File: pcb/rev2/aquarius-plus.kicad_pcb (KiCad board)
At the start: 2 copper layers, 167 x 115 mm, 173 parts, among them J1 Power in, J10 FPGA spare, J11 Hand controller 2, J12 Hand controller 1, J13 ESP32 spare, J2 ESP USB Host, J3 Audio out, J4 VGA, J5 Cassette out, J6 Cassette in, J7 Expansion port, J8 Printer, J9 TF-03A, Q1 BC847C, Q2 BC847C, Q3 2N7002, SW1 SW_DPDT_x2, U1 SN74AHCT1G125DBVR, U10 ESP32-S3-WROOM-1-N4R2, U11 LDL1117S33R, U12 SN74CB3T3245PWR, U13 IS61C5128AS-25QLI, U2 SN74AHCT1G125DBVR, U3 LD1117S12, U4 SN74CB3T3245PWR, U5 MAX3221ECPWR, U6 XC6SLX9-2TQG144C, U7 Z84C0010AEG, U8 SN74CB3T3245PWR, U9 SN74CB3T3245PWR, X1 SX3M14.31818M20F30TNN

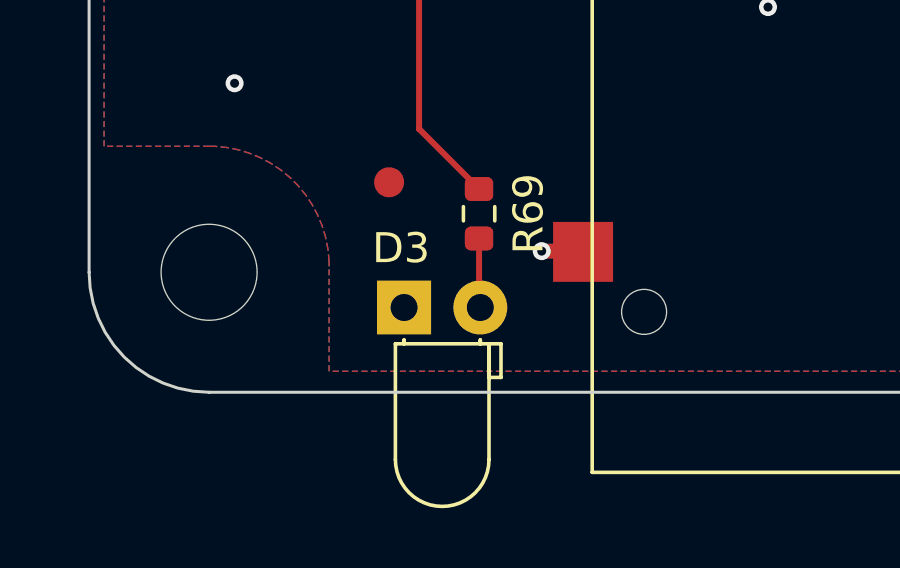
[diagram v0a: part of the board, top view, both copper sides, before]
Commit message: PCB rev2 Tweaks for LED polarity
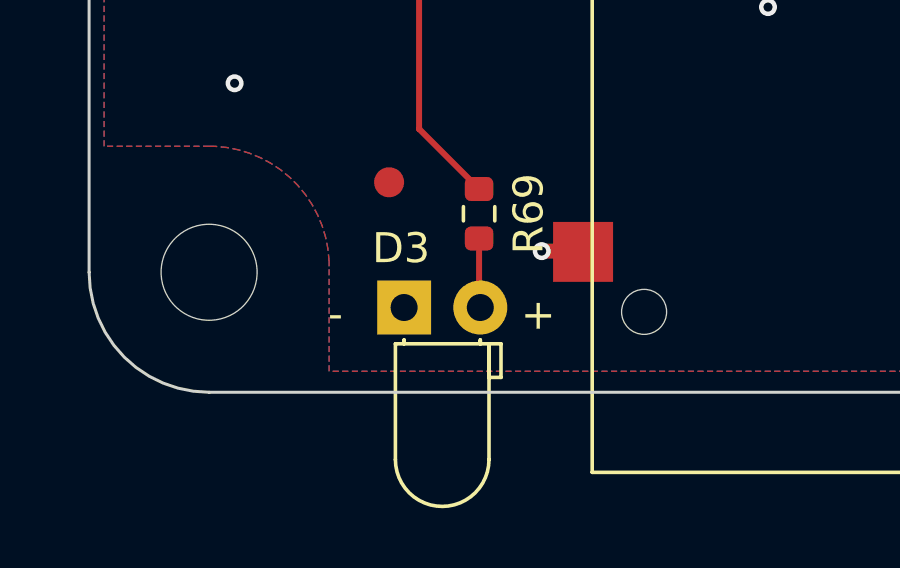
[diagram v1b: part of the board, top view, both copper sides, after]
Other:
- board text added: "+"
- board text added: "-"
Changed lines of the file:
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@@
     (effects (font (size 1.5 1.5) (thickness 0.3)))
+  )
+  (gr_text "-" (at 72.964539 147.399272) (layer "F.SilkS")
+    (effects (font (size 1 1) (thickness 0.15)) (justify left))
   )
   (gr_text "Audio Out" (at 132 47.5 90) (layer "F.SilkS")
@@
     (effects (font (size 2 2) (thickness 0.3)))
   )
+  (gr_text "+" (at 79.395539 147.419623) (layer "F.SilkS")
+    (effects (font (size 1 1) (thickness 0.15)) (justify left))
+  )
   (gr_text "Power" (at 80.133319 42.362823) (layer "F.SilkS")

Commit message: Renaming SPI nets to match the software.
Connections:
- U10 pad 15: SPI_MISO -> SPI_CS#
- U10 pad 19: SPI_CS# -> SPI_MISO
- U6 pad 39: SPI_MISO -> SPI_CS#
- U6 pad 74: SPI_CS# -> SPI_MISO
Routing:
- net SPI_MISO: track 53.2 -> 45.3 mm, vias 4 -> 0
- net SPI_CS#: track 45.3 -> 53.2 mm, vias 0 -> 4
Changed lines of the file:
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@@
       (net 41 "CASSETTE_OUT") (pinfunction "B2_IO") (pintype "passive"))
     (pad "39" smd roundrect (at -7.75 10.6625 270) (size 0.3 1.475) (layers "F.Cu" "F.Paste" "F.Mask") (roundrect_rratio 0.25)
-      (net 96 "SPI_MISO") (pinfunction "B2_IO_INIT_B") (pintype "passive"))
+      (net 28 "SPI_CS#") (pinfunction "B2_IO_INIT_B") (pintype "passive"))
     (pad "40" smd roundrect (at -7.25 10.6625 270) (size 0.3 1.475) (layers "F.Cu" "F.Paste" "F.Mask") (roundrect_rratio 0.25)
       (net 26 "CASSETTE_IN") (pinfunction "B2_IO") (pintype "passive"))
@@
       (net 2 "GND") (pinfunction "SUSPEND") (pintype "input"))
     (pad "74" smd roundrect (at 10.6625 8.25 270) (size 1.475 0.3) (layers "F.Cu" "F.Paste" "F.Mask") (roundrect_rratio 0.25)
-      (net 28 "SPI_CS#") (pinfunction "B2_IO_DOUT") (pintype "passive"))
+      (net 96 "SPI_MISO") (pinfunction "B2_IO_DOUT") (pintype "passive"))
     (pad "75" smd roundrect (at 10.6625 7.75 270) (size 1.475 0.3) (layers "F.Cu" "F.Paste" "F.Mask") (roundrect_rratio 0.25)
       (net 66 "HC1_D00") (pinfunction "B1_IO_AWAKE") (pintype "passive"))
@@
       (net 25 "ESP_USB_D+") (pinfunction "IO20/USB_DP") (pintype "bidirectional"))
     (pad "15" smd roundrect locked (at -6.985 25.25 270) (size 0.9 1.5) (layers "F.Cu" "F.Paste" "F.Mask") (roundrect_rratio 0.25)
-      (net 96 "SPI_MISO") (pinfunction "IO3") (pintype "bidirectional"))
+      (net 28 "SPI_CS#") (pinfunction "IO3") (pintype "bidirectional"))
     (pad "16" smd roundrect locked (at -5.715 25.25 270) (size 0.9 1.5) (layers "F.Cu" "F.Paste" "F.Mask") (roundrect_rratio 0.25)
       (net 243 "unconnected-(U10-IO46{slash}I-Pad16)") (pinfunction "IO46/I") (pintype "input+no_connect"))
@@
       (net 33 "SPI_SCLK") (pinfunction "IO10") (pintype "bidirectional"))
     (pad "19" smd roundrect locked (at -1.905 25.25 270) (size 0.9 1.5) (layers "F.Cu" "F.Paste" "F.Mask") (roundrect_rratio 0.25)
-      (net 28 "SPI_CS#") (pinfunction "IO11") (pintype "bidirectional"))
+      (net 96 "SPI_MISO") (pinfunction "IO11") (pintype "bidirectional"))
     (pad "20" smd roundrect locked (at -0.635 25.25 270) (size 0.9 1.5) (layers "F.Cu" "F.Paste" "F.Mask") (roundrect_rratio 0.25)
       (net 94 "ESP_NOTIFY") (pinfunction "IO12") (pintype "bidirectional"))
@@
   (segment (start 114.400499 84.231011) (end 114.132509 84.499001) (width 0.2) (layer "B.Cu") (net 26))
   (segment (start 88.0125 69.1) (end 83.325 69.1) (width 0.3) (layer "F.Cu") (net 27))
-  (segment (start 126.97 103.875) (end 126.97 104.83) (width 0.2) (layer "F.Cu") (net 28))
-  (segment (start 92.497908 107.905) (end 90.25 107.905) (width 0.2) (layer "F.Cu") (net 28))
-  (segment (start 116.41498 100.4) (end 113.46498 97.45) (width 0.2) (layer "F.Cu") (net 28))
-  (segment (start 118.353218 100.4) (end 116.41498 100.4) (width 0.2) (layer "F.Cu") (net 28))
-  (segment (start 125.75 105.1) (end 124.75 104.1) (width 0.2) (layer "F.Cu") (net 28))
-  (segment (start 126.97 104.83) (end 126.7 105.1) (width 0.2) (layer "F.Cu") (net 28))
-  (segment (start 102.952908 97.45) (end 92.497908 107.905) (width 0.2) (layer "F.Cu") (net 28))
-  (segment (start 126.7 105.1) (end 125.75 105.1) (width 0.2) (layer "F.Cu") (net 28))
-  (segment (start 122.053218 104.1) (end 118.353218 100.4) (width 0.2) (layer "F.Cu") (net 28))
-  (segment (start 113.46498 97.45) (end 102.952908 97.45) (width 0.2) (layer "F.Cu") (net 28))
-  (segment (start 124.75 104.1) (end 122.053218 104.1) (width 0.2) (layer "F.Cu") (net 28))
+  (segment (start 124.5575 85.4625) (end 123.0625 85.4625) (width 0.2) (layer "F.Cu") (net 28))
+  (segment (start 113.7 85.8) (end 110.6 85.8) (width 0.2) (layer "F.Cu") (net 28))
+  (segment (start 90.25 112.985) (end 91.55 112.985) (width 0.2) (layer "F.Cu") (net 28))
+  (segment (start 123.0625 85.4625) (end 122.9 85.3) (width 0.2) (layer "F.Cu") (net 28))
+  (segment (start 116.5005 85.3) (end 116.3 85.0995) (width 0.2) (layer "F.Cu") (net 28))
+  (segment (start 110.6 85.8) (end 96.55 99.85) (width 0.2) (layer "F.Cu") (net 28))
+  (segment (start 96.55 99.85) (end 93.15 99.85) (width 0.2) (layer "F.Cu") (net 28))
+  (segment (start 122.9 85.3) (end 116.5005 85.3) (width 0.2) (layer "F.Cu") (net 28))
+  (segment (start 93.15 99.85) (end 92.95 99.65) (width 0.2) (layer "F.Cu") (net 28))
+  (via (at 113.7 85.8) (size 0.6) (drill 0.3) (layers "F.Cu" "B.Cu") (net 28))
+  (via (at 116.3 85.0995) (size 0.6) (drill 0.3) (layers "F.Cu" "B.Cu") (net 28))
+  (via (at 91.55 112.985) (size 0.6) (drill 0.3) (layers "F.Cu" "B.Cu") (net 28))
+  (via (at 92.95 99.65) (size 0.6) (drill 0.3) (layers "F.Cu" "B.Cu") (net 28))
+  (segment (start 113.7 85.8) (end 115.5995 85.8) (width 0.2) (layer "B.Cu") (net 28))
+  (segment (start 92.95 99.65) (end 92.95 111.585) (width 0.2) (layer "B.Cu") (net 28))
+  (segment (start 92.95 111.585) (end 91.55 112.985) (width 0.2) (layer "B.Cu") (net 28))
+  (segment (start 115.5995 85.8) (end 116.3 85.0995) (width 0.2) (layer "B.Cu") (net 28))
   (segment (start 84.75 125.4) (end 83.8414 124.4914) (width 0.2) (layer "F.Cu") (net 29))
   (segment (start 98.28 123.07) (end 98.28 124.42) (width 0.2) (layer "F.Cu") (net 29))
@@
   (segment (start 123.3875 93.4625) (end 122.87 93.98) (width 0.2) (layer "F.Cu") (net 95))
   (segment (start 124.5575 93.4625) (end 123.3875 93.4625) (width 0.2) (layer "F.Cu") (net 95))
-  (segment (start 124.5575 85.4625) (end 123.0625 85.4625) (width 0.2) (layer "F.Cu") (net 96))
-  (segment (start 113.7 85.8) (end 110.6 85.8) (width 0.2) (layer "F.Cu") (net 96))
-  (segment (start 90.25 112.985) (end 91.55 112.985) (width 0.2) (layer "F.Cu") (net 96))
-  (segment (start 123.0625 85.4625) (end 122.9 85.3) (width 0.2) (layer "F.Cu") (net 96))
-  (segment (start 116.5005 85.3) (end 116.3 85.0995) (width 0.2) (layer "F.Cu") (net 96))
-  (segment (start 110.6 85.8) (end 96.55 99.85) (width 0.2) (layer "F.Cu") (net 96))
-  (segment (start 96.55 99.85) (end 93.15 99.85) (width 0.2) (layer "F.Cu") (net 96))
-  (segment (start 122.9 85.3) (end 116.5005 85.3) (width 0.2) (layer "F.Cu") (net 96))
-  (segment (start 93.15 99.85) (end 92.95 99.65) (width 0.2) (layer "F.Cu") (net 96))
-  (via (at 113.7 85.8) (size 0.6) (drill 0.3) (layers "F.Cu" "B.Cu") (net 96))
-  (via (at 116.3 85.0995) (size 0.6) (drill 0.3) (layers "F.Cu" "B.Cu") (net 96))
-  (via (at 91.55 112.985) (size 0.6) (drill 0.3) (layers "F.Cu" "B.Cu") (net 96))
-  (via (at 92.95 99.65) (size 0.6) (drill 0.3) (layers "F.Cu" "B.Cu") (net 96))
-  (segment (start 113.7 85.8) (end 115.5995 85.8) (width 0.2) (layer "B.Cu") (net 96))
-  (segment (start 92.95 99.65) (end 92.95 111.585) (width 0.2) (layer "B.Cu") (net 96))
-  (segment (start 92.95 111.585) (end 91.55 112.985) (width 0.2) (layer "B.Cu") (net 96))
-  (segment (start 115.5995 85.8) (end 116.3 85.0995) (width 0.2) (layer "B.Cu") (net 96))
+  (segment (start 126.97 103.875) (end 126.97 104.83) (width 0.2) (layer "F.Cu") (net 96))
+  (segment (start 92.497908 107.905) (end 90.25 107.905) (width 0.2) (layer "F.Cu") (net 96))
+  (segment (start 116.41498 100.4) (end 113.46498 97.45) (width 0.2) (layer "F.Cu") (net 96))
+  (segment (start 118.353218 100.4) (end 116.41498 100.4) (width 0.2) (layer "F.Cu") (net 96))
+  (segment (start 125.75 105.1) (end 124.75 104.1) (width 0.2) (layer "F.Cu") (net 96))
+  (segment (start 126.97 104.83) (end 126.7 105.1) (width 0.2) (layer "F.Cu") (net 96))
+  (segment (start 102.952908 97.45) (end 92.497908 107.905) (width 0.2) (layer "F.Cu") (net 96))
+  (segment (start 126.7 105.1) (end 125.75 105.1) (width 0.2) (layer "F.Cu") (net 96))
+  (segment (start 122.053218 104.1) (end 118.353218 100.4) (width 0.2) (layer "F.Cu") (net 96))
+  (segment (start 113.46498 97.45) (end 102.952908 97.45) (width 0.2) (layer "F.Cu") (net 96))
+  (segment (start 124.75 104.1) (end 122.053218 104.1) (width 0.2) (layer "F.Cu") (net 96))
   (segment (start 95 106.532868) (end 100.237198 101.29567) (width 0.2) (layer "F.Cu") (net 97))
   (segment (start 94.005 110.445) (end 95 109.45) (width 0.2) (layer "F.Cu") (net 97))
